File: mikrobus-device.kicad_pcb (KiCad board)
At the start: 2 copper layers, 25.4 x 57.2 mm, 2 parts, among them J1 Conn_01x08, J2 Conn_01x08

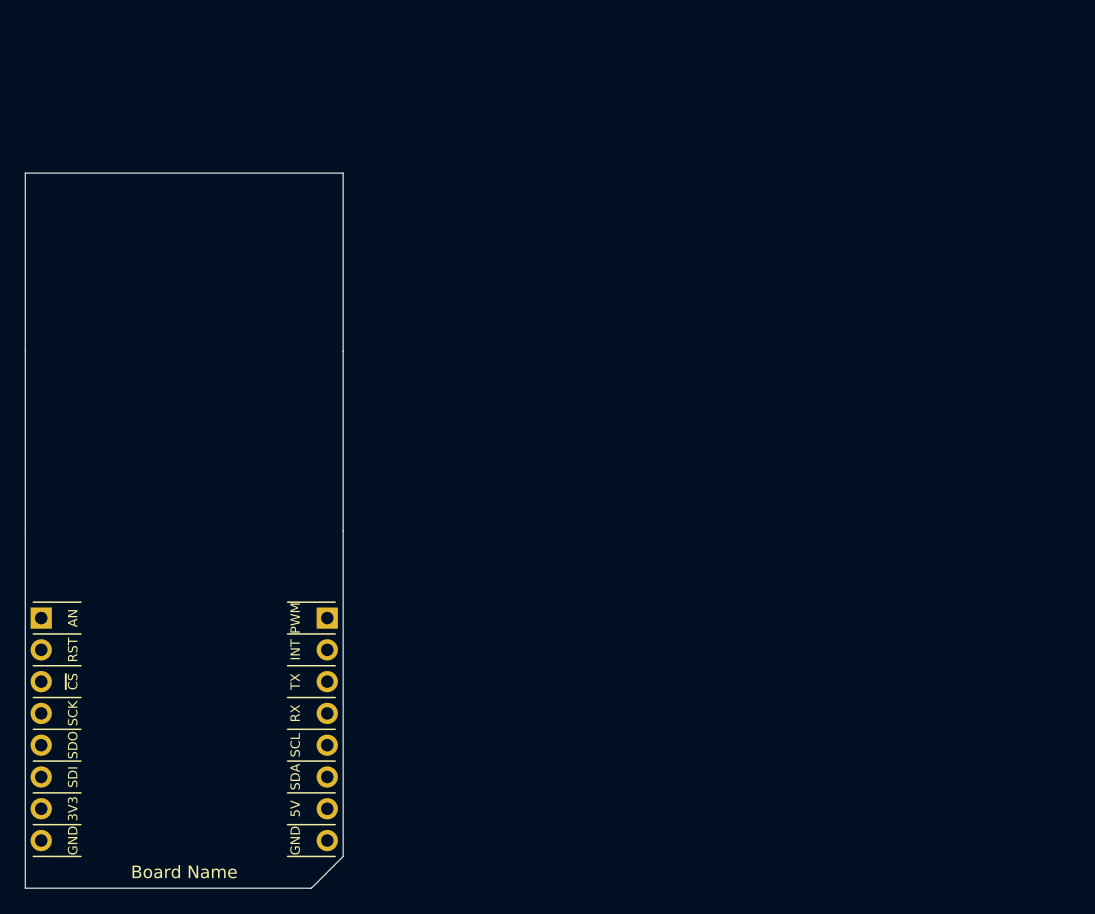
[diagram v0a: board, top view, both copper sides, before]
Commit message: actualizando a kicad 7
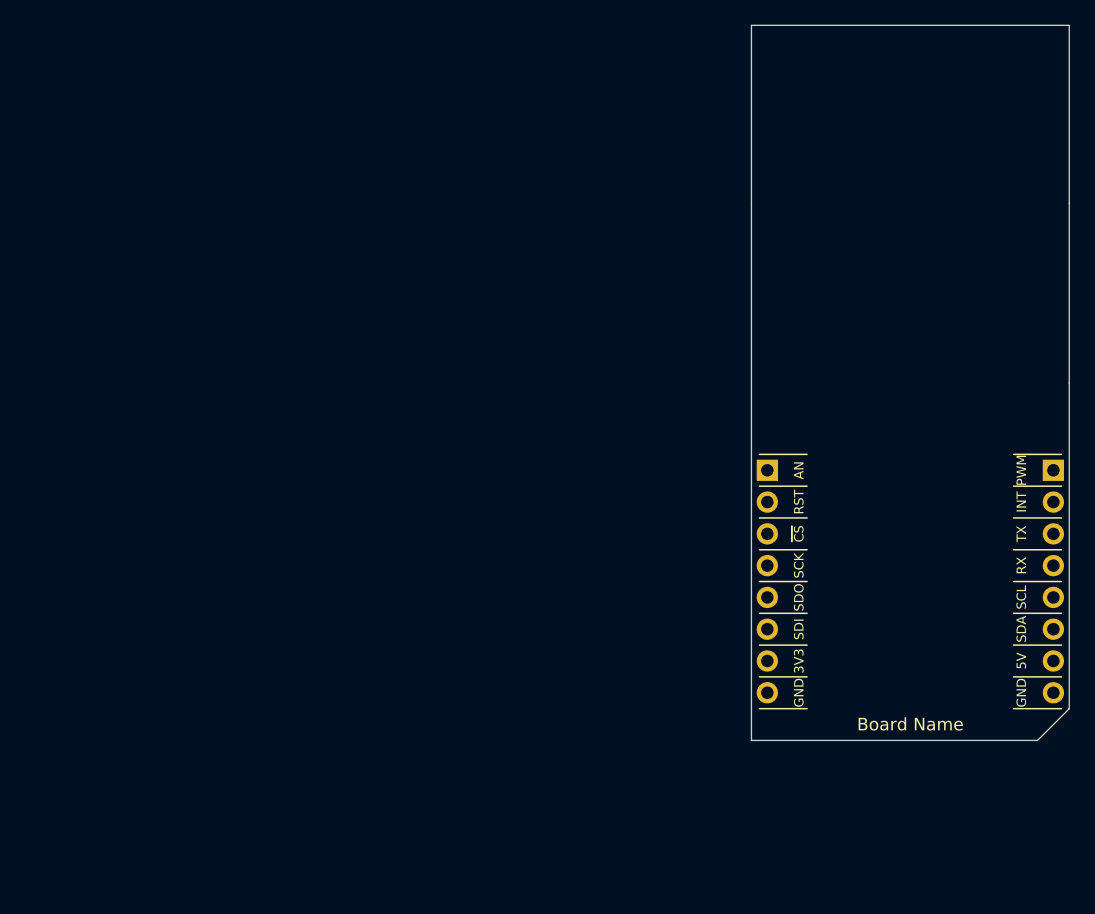
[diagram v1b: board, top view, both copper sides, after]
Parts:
- moved J1 59.2 mm to (136.8, 97.4)
- moved J2 59.2 mm to (159.6, 97.4)
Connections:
- net /~CS~ renamed /~{CS}
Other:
- board size 25.4 x 57.2 mm -> 25.4 x 57.1 mm
- net class Default removed
- board text added: "~{CS}"
- board text removed: "~CS~"
